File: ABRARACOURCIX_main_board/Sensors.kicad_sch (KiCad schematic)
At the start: 31 parts, among them U1 STM32F429ZIT6, U2 ICM-42688-P, U5 BNO055, Y1 32.768kHz

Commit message: Reprise de contrôle
Schematics terminés
Reste à associer des composantes et vérification
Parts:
- removed U2: ICM-42688-P, ICM-42688-P:PQFN50P300X250X97-14N, symbol GAUL_ABRARACOURCIX1:ICM-42688-P
- added TP4, TP5: TestPoint, symbol Connector:TestPoint
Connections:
- net I2C_SELECT is gone; now on net GND: U5.17 (COM3)
- net SCL: now also TP5.1
- net SDA: now also TP4.1
- net BNO_BL_IND: no longer names the net of U5.10 (PIN10)
- no-connect marks 2 -> 3

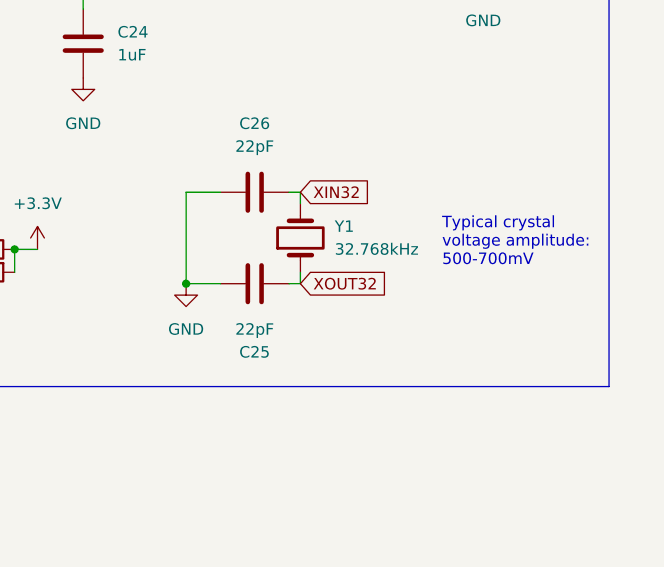
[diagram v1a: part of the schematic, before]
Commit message: Assignation d<empreintes terminée
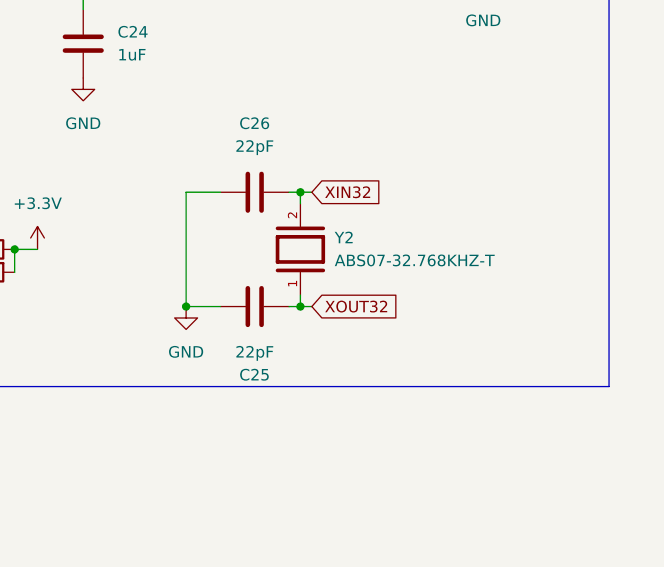
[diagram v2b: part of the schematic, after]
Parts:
- removed Y1: 32.768kHz, symbol Device:Crystal
- added Y2: ABS07-32.768KHZ-T, Librairie_footprint:XTAL_ABS07-32.768KHZ-T, symbol GAUL_ABRARACOURCIX:ABS07-32.768KHZ-T
- C10, C11, C12, C13, C14, C15, C16, C17, C18, C19, C20, C21, C22, C23, C24, C25, C26, C4, C5, C6, C7, C8, C9: footprint (none) -> Capacitor_SMD:C_1206_3216Metric_Pad1.33x1.80mm_HandSolder
- R10, R5, R6, R7: footprint (none) -> Resistor_SMD:R_1206_3216Metric_Pad1.30x1.75mm_HandSolder
- TP4, TP5: footprint (none) -> TestPoint:TestPoint_THTPad_2.0x2.0mm_Drill1.0mm
- U1: footprint STM32F429ZIT6:QFP50P2200X2200X160-144N -> Librairie_footprint:QFP50P2200X2200X160-144N
- U5: footprint BNO055:LGA28R50P4X10_380X520X100 -> Librairie_footprint:BNO055_LGA28R50P4X10_380X520X100
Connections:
- net XIN32: now also Y2.2
- net XOUT32: now also Y2.1
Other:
- note removed: "Typical crystal voltage amplitude: 500-700mV"
- moved on the sheet: C25
